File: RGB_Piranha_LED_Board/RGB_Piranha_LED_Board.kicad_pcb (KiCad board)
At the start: 2 copper layers, 101.6 x 12.7 mm, 0 parts

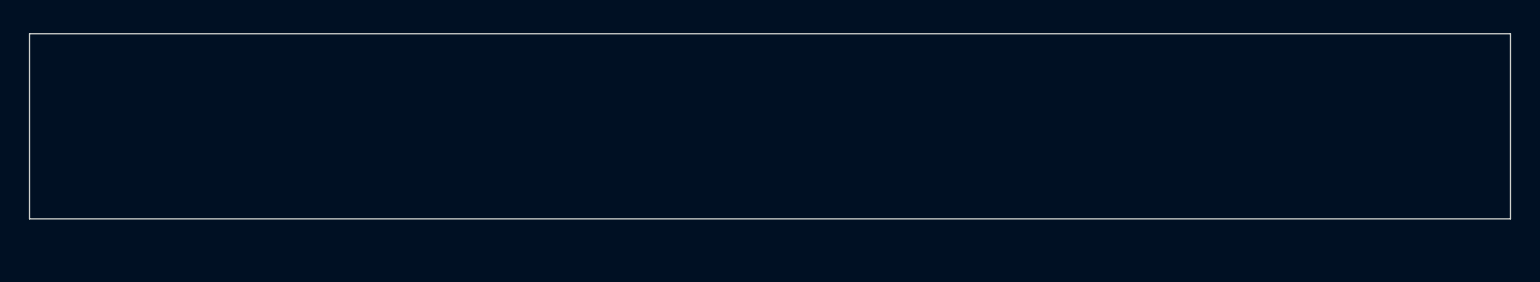
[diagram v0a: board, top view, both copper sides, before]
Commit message: changed THT resistors to SMD
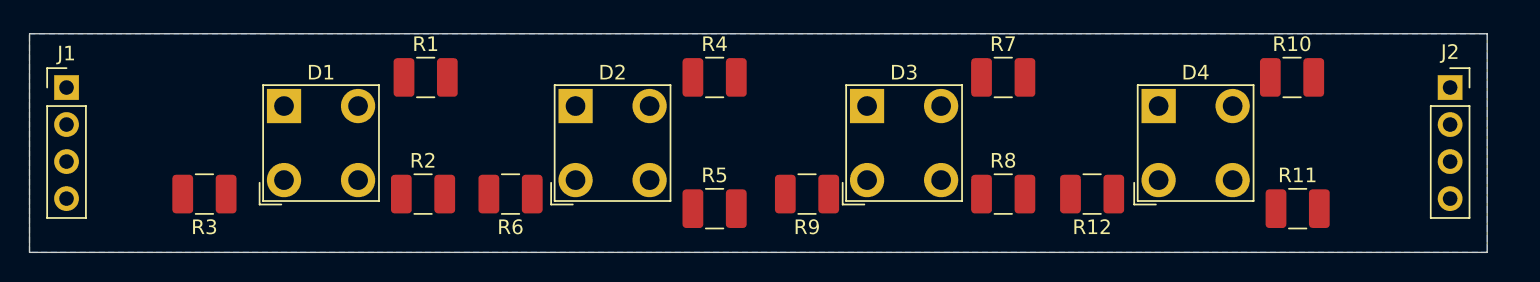
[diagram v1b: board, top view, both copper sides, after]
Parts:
- added D1: LED_ARGB, RGB LED Piranha Super-Flux:LED_FD-115TRGB-A2, F.Cu at (20.0, 7.50)
- added D2: LED_ARGB, RGB LED Piranha Super-Flux:LED_FD-115TRGB-A2, F.Cu at (40.0, 7.50)
- added D3: LED_ARGB, RGB LED Piranha Super-Flux:LED_FD-115TRGB-A2, F.Cu at (60.0, 7.50)
- added D4: LED_ARGB, RGB LED Piranha Super-Flux:LED_FD-115TRGB-A2, F.Cu at (80.0, 7.50)
- added J1: Conn_IN, Connector_PinHeader_2.54mm:PinHeader_1x04_P2.54mm_Vertical, F.Cu at (2.54, 3.69)
- added J2: Conn_OUT, Connector_PinSocket_2.54mm:PinSocket_1x04_P2.54mm_Vertical, F.Cu at (97.5, 3.69)
- added R1: 620, Resistor_SMD:R_1210_3225Metric_Pad1.42x2.65mm_HandSolder, F.Cu at (27.2, 3.00)
- added R10: 620, Resistor_SMD:R_1210_3225Metric_Pad1.42x2.65mm_HandSolder, F.Cu at (86.6, 3.00)
- added R11: 620, Resistor_SMD:R_1210_3225Metric_Pad1.42x2.65mm_HandSolder, F.Cu at (87.0, 12.0)
- added R12: 620, Resistor_SMD:R_1210_3225Metric_Pad1.42x2.65mm_HandSolder, F.Cu at (72.9, 11.0)
- added R2: 620, Resistor_SMD:R_1210_3225Metric_Pad1.42x2.65mm_HandSolder, F.Cu at (27.0, 11.0)
- added R3: 620, Resistor_SMD:R_1210_3225Metric_Pad1.42x2.65mm_HandSolder, F.Cu at (12.0, 11.0)
- added R4: 620, Resistor_SMD:R_1210_3225Metric_Pad1.42x2.65mm_HandSolder, F.Cu at (47.0, 3.00)
- added R5: 620, Resistor_SMD:R_1210_3225Metric_Pad1.42x2.65mm_HandSolder, F.Cu at (47.0, 12.0)
- added R6: 620, Resistor_SMD:R_1210_3225Metric_Pad1.42x2.65mm_HandSolder, F.Cu at (33.0, 11.0)
- added R7: 620, Resistor_SMD:R_1210_3225Metric_Pad1.42x2.65mm_HandSolder, F.Cu at (66.8, 3.00)
- added R8: 620, Resistor_SMD:R_1210_3225Metric_Pad1.42x2.65mm_HandSolder, F.Cu at (66.8, 11.0)
- added R9: 620, Resistor_SMD:R_1210_3225Metric_Pad1.42x2.65mm_HandSolder, F.Cu at (53.3, 11.0)
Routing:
- added copper zone on B.Cu, net +12V
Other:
- board size 101.6 x 12.7 mm -> 100 x 15 mm
- net class Default: trace_width 0.25 -> 1

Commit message: some changes
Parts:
- moved R10 2.01 mm to (87.0, 4.96)
- moved R7 1.97 mm to (67.0, 4.96)
- moved R1 1.96 mm to (27.0, 4.96)
- moved R11 1.96 mm to (87.0, 10.0)
- moved R5 1.96 mm to (47.0, 10.0)
- moved R4 1.96 mm to (47.0, 4.96)
- moved R3 1.36 mm to (13.0, 10.0)
- moved R9 1.03 mm to (53.0, 10.0)
- moved R8 0.99 mm to (67.0, 10.0)
- moved R12 0.96 mm to (73.0, 10.0)
- moved R2 0.96 mm to (27.0, 10.0)
- moved R6 0.96 mm to (33.0, 10.0)

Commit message: generated gerbers
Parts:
- moved D1 141.4 mm to (120.0, 107.5)
- moved D2 141.4 mm to (140.0, 107.5)
- moved D3 141.4 mm to (160.0, 107.5)
- moved D4 141.4 mm to (180.0, 107.5)
- moved J1 141.4 mm to (102.5, 103.7)
- moved J2 141.4 mm to (197.5, 103.7)
- moved R1 141.4 mm to (127.0, 105.0)
- moved R12 141.4 mm to (173.0, 110.0)
- moved R2 141.4 mm to (127.0, 110.0)
- moved R3 141.4 mm to (113.0, 110.0)
- moved R4 141.4 mm to (147.0, 105.0)
- moved R5 141.4 mm to (147.0, 110.0)
- moved R6 141.4 mm to (133.0, 110.0)
- moved R9 141.4 mm to (153.0, 110.0)
- moved R10 141.4 mm to (187.0, 105.0)
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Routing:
- net Net-(J1-Pad2): track 0.00 -> 110.3 mm
- net Net-(J1-Pad4): track 0.00 -> 108.2 mm
- net Net-(J1-Pad3): track 0.00 -> 106.1 mm
- net Net-(D4-Pad4): track 0.00 -> 3.01 mm
- net Net-(D4-Pad3): track 0.00 -> 3.01 mm
- net Net-(D4-Pad2): track 0.00 -> 3.01 mm
- net Net-(D3-Pad4): track 0.00 -> 3.01 mm
- net Net-(D3-Pad3): track 0.00 -> 3.01 mm
- net Net-(D3-Pad2): track 0.00 -> 3.01 mm
- net Net-(D2-Pad4): track 0.00 -> 3.01 mm
- net Net-(D2-Pad3): track 0.00 -> 3.01 mm
- net Net-(D2-Pad2): track 0.00 -> 3.01 mm
- net Net-(D1-Pad4): track 0.00 -> 3.01 mm
- net Net-(D1-Pad3): track 0.00 -> 3.01 mm
- net Net-(D1-Pad2): track 0.00 -> 3.01 mm
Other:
- board text added: "RGB Piranha LED / DMA'23"
